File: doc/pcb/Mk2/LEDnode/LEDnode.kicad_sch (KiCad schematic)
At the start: 76 parts, among them J1 Ni-MH, J2 SWD, J4 GPIO2, Q1 PDTB113ET.215, Q2 PDTB113ET.215, Q3 PDTB113ET.215, Q4 PDTB113ET.215, Q5 IRLML6346, Q6 BSS138, Q7 IRLML6346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

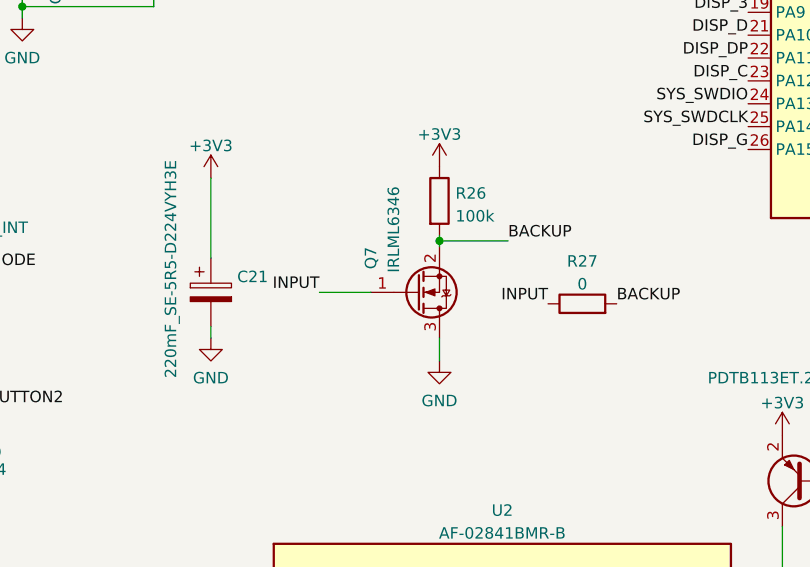
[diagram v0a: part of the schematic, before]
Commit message: corrected backup transistor
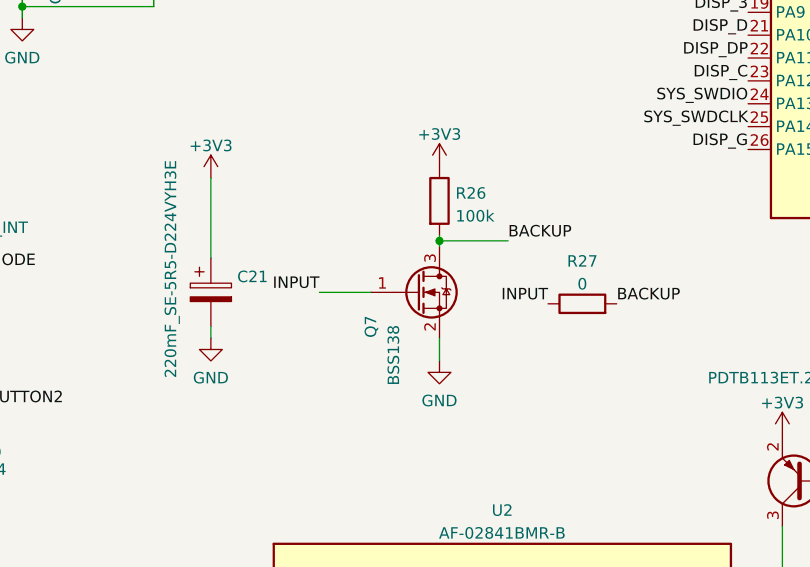
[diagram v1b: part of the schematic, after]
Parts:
- Q7: value IRLML6346 -> BSS138
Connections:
- net BACKUP: now also Q7.3 (D); no longer Q7.2 (S)
- net GND: now also Q7.2 (S); no longer Q7.3 (D)
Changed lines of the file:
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@@
     (pin "3")
   )
-  (symbol (lib_id "Device:Q_NMOS_GSD") (at 103.505 134.62 0) (mirror x) (unit 1)
-    (in_bom yes) (on_board yes)
-    (property "Reference" "Q7" (id 0) (at 98.425 130.81 90))
-    (property "Value" "IRLML6346" (id 1) (at 100.965 127.635 90))
-    (property "Footprint" "Package_TO_SOT_SMD:SOT-23" (id 2) (at 108.585 137.16 0)
+  (symbol (lib_id "Device:Q_NMOS_GSD") (at 103.505 134.62 0) (unit 1)
+    (in_bom yes) (on_board yes)
+    (property "Reference" "Q7" (id 0) (at 98.425 138.43 90))
+    (property "Value" "BSS138" (id 1) (at 100.965 141.605 90))
+    (property "Footprint" "Package_TO_SOT_SMD:SOT-23" (id 2) (at 108.585 132.08 0)
       (effects (font (size 1.27 1.27)) hide)
     )
@@
     )
     (path "/d758ce62-ce56-4102-99f3-1a8e22ed504c"
-      (reference "Q7") (unit 1) (value "IRLML6346") (footprint "Package_TO_SOT_SMD:SOT-23")
+      (reference "Q7") (unit 1) (value "BSS138") (footprint "Package_TO_SOT_SMD:SOT-23")
     )
     (path "/90f62ab4-3b57-4e43-92c1-505510d0ded2"

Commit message: 1.4
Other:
- note added: "Changelog: 1.1- corrected Q7 symbol"
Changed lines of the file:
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@@
+    (effects (font (size 1.27 1.27)) (justify left bottom))
+  )
+  (text "Changelog:\n1.1- corrected Q7 symbol" (at 180.975 172.72 0)
     (effects (font (size 1.27 1.27)) (justify left bottom))
   )
@@
       (effects (font (size 1.27 1.27)) (justify left))
     )
-    (property "Value" "MCU_INT" (id 1) (at 37.465 127 0)
-      (effects (font (size 1.27 1.27)) (justify left))
-    )
+    (property "Value" "MCU_INT" (id 1) (at 34.29 127 0)
+      (effects (font (size 1.27 1.27)) (justify left))
+    )

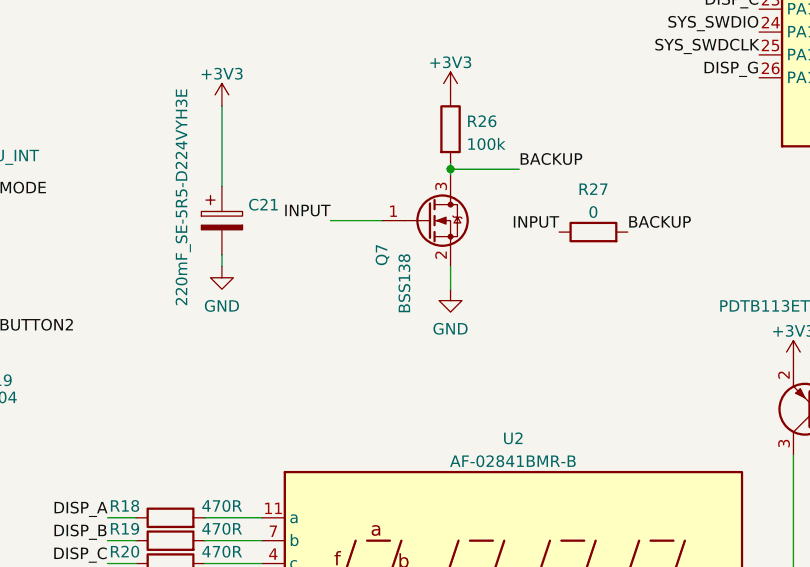
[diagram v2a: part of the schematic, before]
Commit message: magnetometer support
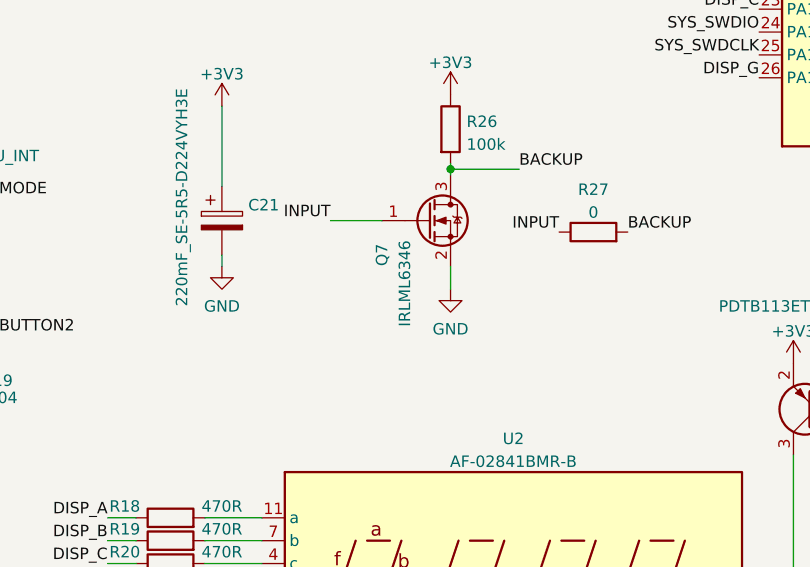
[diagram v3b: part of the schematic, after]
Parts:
- Q7: value BSS138 -> IRLML6346
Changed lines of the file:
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@@
     (in_bom yes) (on_board yes)
     (property "Reference" "Q7" (id 0) (at 98.425 138.43 90))
-    (property "Value" "BSS138" (id 1) (at 100.965 141.605 90))
+    (property "Value" "IRLML6346" (id 1) (at 100.965 141.605 90))
     (property "Footprint" "Package_TO_SOT_SMD:SOT-23" (id 2) (at 108.585 132.08 0)
       (effects (font (size 1.27 1.27)) hide)
@@
     )
     (path "/d758ce62-ce56-4102-99f3-1a8e22ed504c"
-      (reference "Q7") (unit 1) (value "BSS138") (footprint "Package_TO_SOT_SMD:SOT-23")
+      (reference "Q7") (unit 1) (value "IRLML6346") (footprint "Package_TO_SOT_SMD:SOT-23")
     )
     (path "/90f62ab4-3b57-4e43-92c1-505510d0ded2"
